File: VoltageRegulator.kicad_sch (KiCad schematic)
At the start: 16 parts, among them J1 Conn_01x02_Female, Q1 VNP10N07

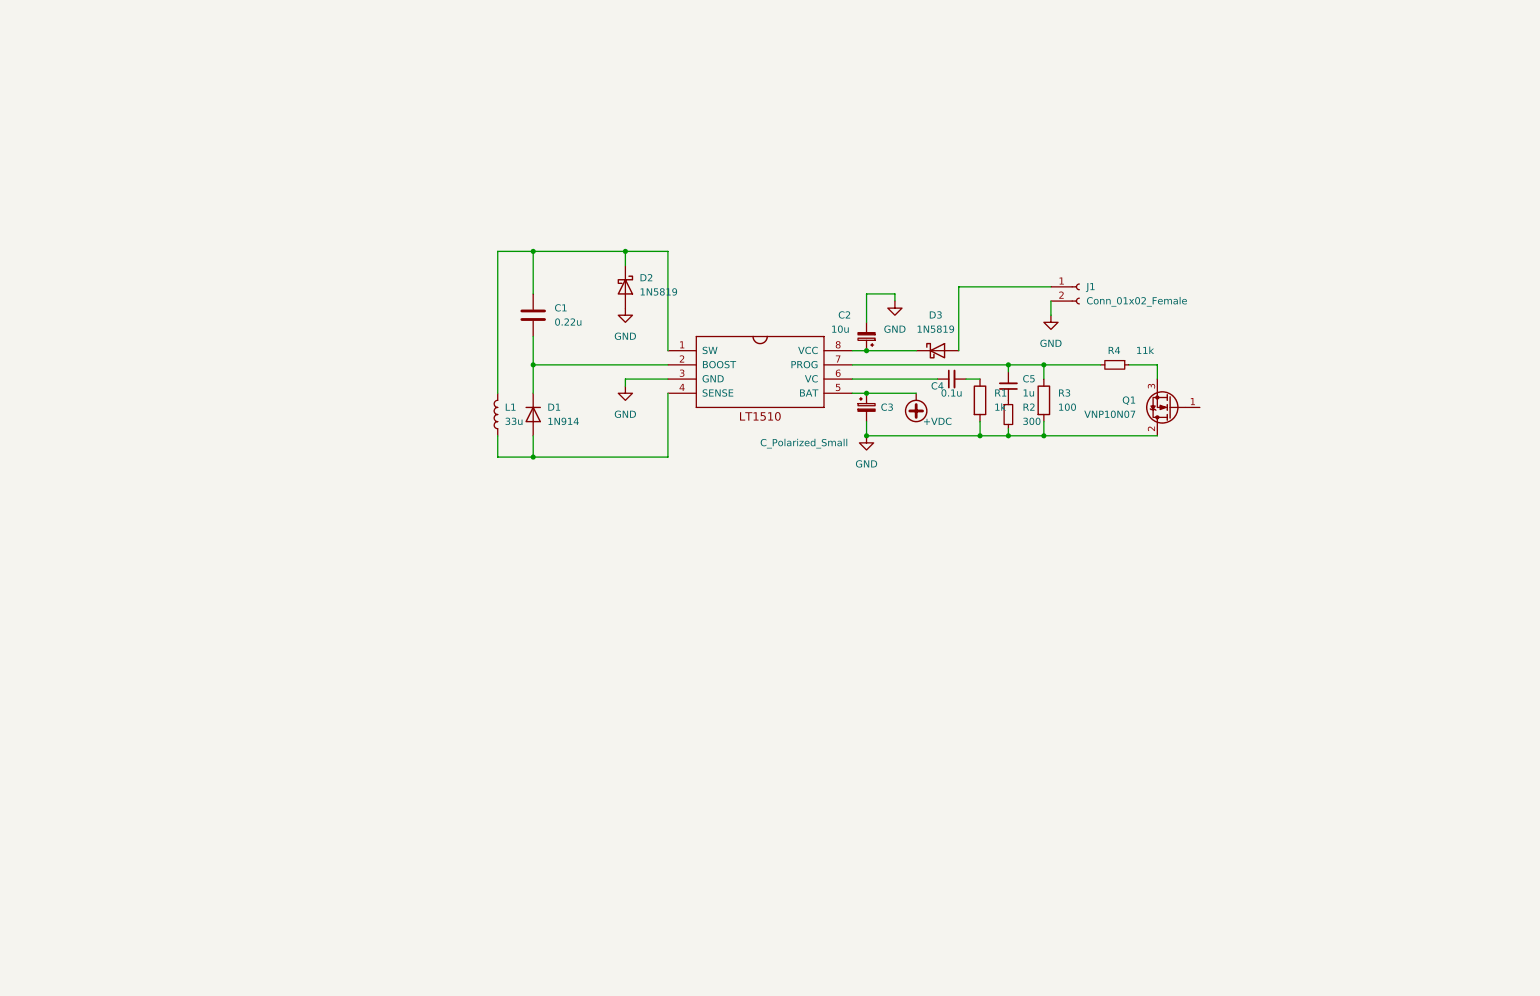
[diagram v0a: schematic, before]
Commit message: Layout almost finished
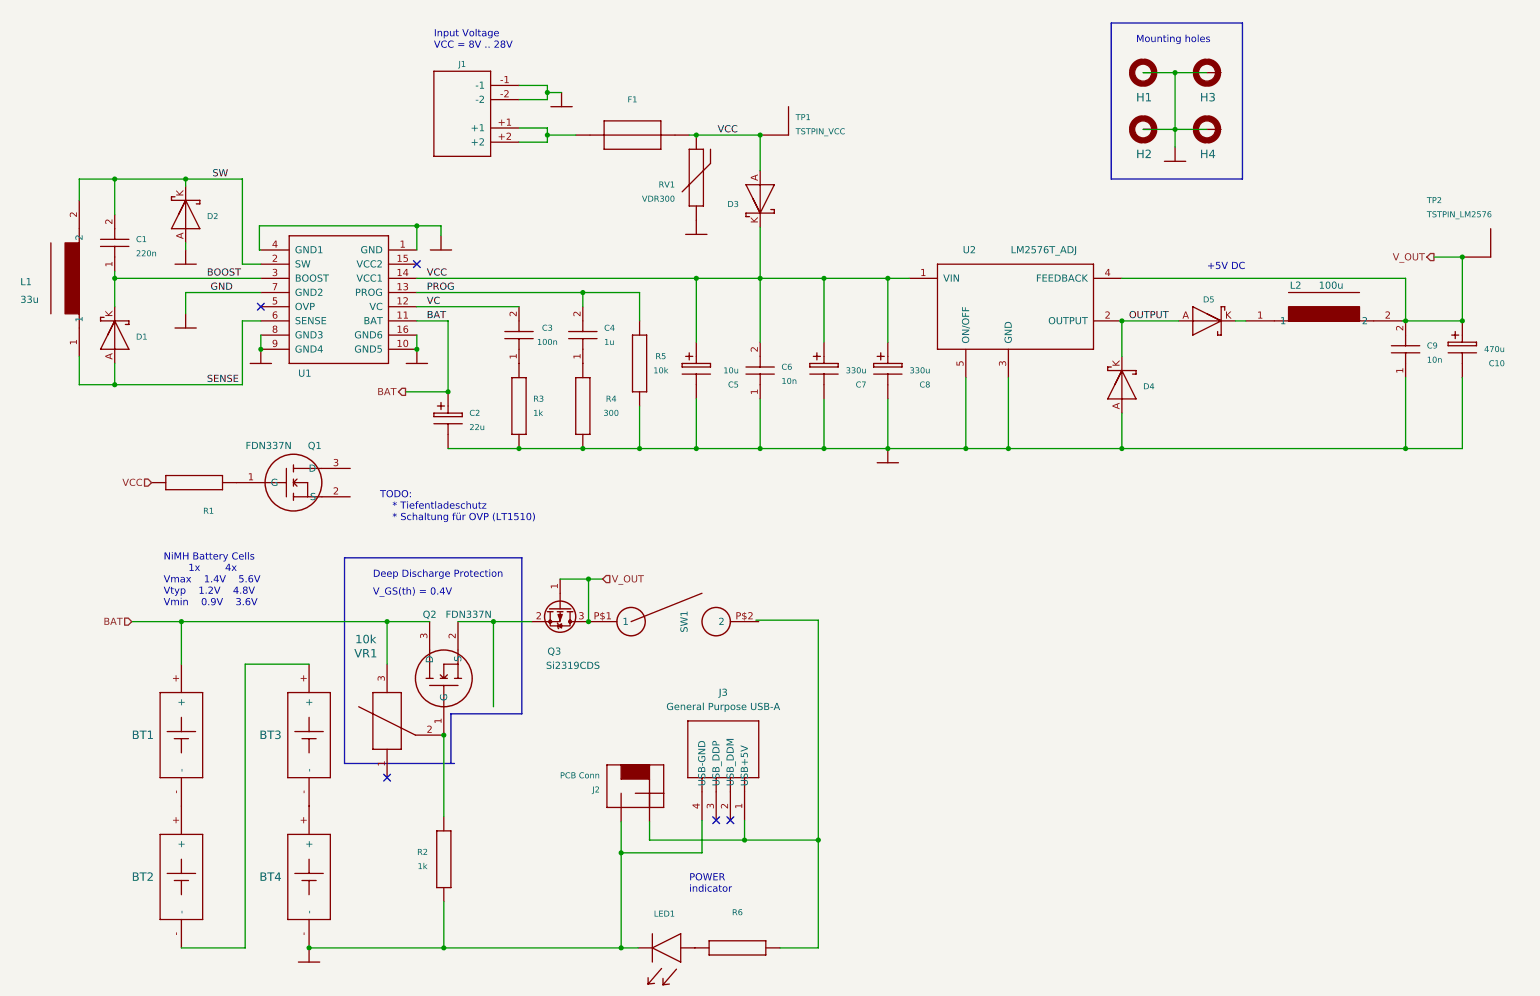
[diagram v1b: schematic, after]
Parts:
- removed 1: LT1510, symbol EmbeddedSys:LT1510
- removed C1: 0.22u, Capacitor_SMD:C_0603_1608Metric, symbol Device:C
- removed C2: 10u, Capacitor_SMD:C_0603_1608Metric, symbol Device:C_Polarized_Small
- removed C3: C_Polarized_Small, symbol Device:C_Polarized_Small
- removed C4: 0.1u, Capacitor_SMD:C_0603_1608Metric, symbol Device:C_Small
- removed C5: 1u, Capacitor_SMD:C_0603_1608Metric, symbol Device:C_Small
- removed D1: 1N914, Diode_THT:D_DO-35_SOD27_P7.62mm_Horizontal, symbol Diode:1N914
- removed D2, D3: 1N5819, Diode_THT:D_DO-41_SOD81_P10.16mm_Horizontal, symbol Diode:1N5819
- removed J1: Conn_01x02_Female, Connector_JST:JST_EH_B2B-EH-A_1x02_P2.50mm_Vertical, symbol Connector:Conn_01x02_Female
- removed L1: 33u, Capacitor_SMD:C_0603_1608Metric, symbol Device:L
- removed Q1: VNP10N07, Package_TO_SOT_THT:TO-220-3_Vertical, symbol Transistor_FET:VNP10N07
- removed R1: 1k, Resistor_SMD:R_0603_1608Metric, symbol Device:R
- removed R2: 300, Resistor_SMD:R_0603_1608Metric, symbol Device:R_Small
- removed R3: 100, Resistor_SMD:R_0603_1608Metric, symbol Device:R
- removed R4: 11k, Resistor_SMD:R_0603_1608Metric, symbol Device:R_Small
- added BT1, BT2, BT3, BT4: POWER_POWER_AKKU, LIB_Embedsys:POWER_POWER_AKKU_AA, symbol EmbeddedSys:POWER_POWER_AKKU
- added C1: 220n, LIB_Embedsys:C1206, symbol EmbeddedSys:POWER_POWER_C_SMD
- added C10: 470u, LIB_Embedsys:POWER_POWER_C-POL, symbol EmbeddedSys:POWER_POWER_C-POL{dblquote}
- added C2: 22u, LIB_Embedsys:POWER_POWER_C-POL, symbol EmbeddedSys:POWER_POWER_C-POL{dblquote}
- added C3: 100n, LIB_Embedsys:C1206, symbol EmbeddedSys:POWER_POWER_C_SMD
- added C4: 1u, LIB_Embedsys:C1206, symbol EmbeddedSys:POWER_POWER_C_SMD
- added C5: 10u, LIB_Embedsys:POWER_POWER_C-POL, symbol EmbeddedSys:POWER_POWER_C-POL{dblquote}
- added C6, C9: 10n, LIB_Embedsys:C1206, symbol EmbeddedSys:POWER_POWER_C_SMD
- added C7, C8: 330u, LIB_Embedsys:POWER_POWER_C-POL, symbol EmbeddedSys:POWER_POWER_C-POL{dblquote}
- added D1, D2, D3, D4, D5: POWER_POWER_SB560", LIB_Embedsys:POWER_POWER_DO201AD, symbol EmbeddedSys:POWER_POWER_SB560{dblquote}
- added F1: (no value), symbol EmbeddedSys:POWER_POWER_FUSE{dblquote}
- added H1, H2, H3, H4: MOUNT-PAD-3.0, LIB_Embedsys:POWER_HOLES_3,0-PAD, symbol EmbeddedSys:POWER_HOLES_MOUNT-PAD-ROUND3.0
- added J1: POWER_POWER_ROKA-PWR-IN, LIB_Embedsys:POWER_POWER_ROKA-PWR-IN, symbol EmbeddedSys:POWER_POWER_ROKA-PWR-IN
- added J2: PCB Conn, LIB_Embedsys:POWER_POWER_CON2, symbol EmbeddedSys:POWER_POWER_CON2{dblquote}
- added J3: General Purpose USB-A, LIB_Embedsys:POWER_POWER_USBA, symbol EmbeddedSys:POWER_POWER_USBA
- added L1: 33u, LIB_Embedsys:POWER_POWER_SPULE_STEHEND, symbol EmbeddedSys:POWER_POWER_SPULE_STEHEND
- added L2: 100u, LIB_Embedsys:POWER_POWER_SPULE_STEHEND, symbol EmbeddedSys:POWER_POWER_SPULE_STEHEND
- added LED1: (no value), symbol EmbeddedSys:POWER_POWER_LED-3MM
- added Q1, Q2: FDN337N, LIB_Embedsys:SOT23, symbol EmbeddedSys:FDN337N
- added Q3: Si2319CDS, Package_TO_SOT_SMD:SOT-23, symbol Transistor_FET:Si2319CDS
- added R1: (no value), LIB_Embedsys:R0805, symbol EmbeddedSys:POWER_POWER_SMD_R
- added R2, R3: 1k, LIB_Embedsys:R0805, symbol EmbeddedSys:POWER_POWER_SMD_R
- added R4: 300, LIB_Embedsys:R0805, symbol EmbeddedSys:POWER_POWER_SMD_R
- added R5: 10k, LIB_Embedsys:R0805, symbol EmbeddedSys:POWER_POWER_SMD_R
- added R6: (no value), symbol EmbeddedSys:POWER_POWER_SMD_R
- added RV1: VDR300, LIB_Embedsys:POWER_POWER_VDR, symbol EmbeddedSys:POWER_POWER_VDR300
- added SW1: POWER Switch, LIB_Embedsys:POWER_POWER_SWITCH_ON, symbol EmbeddedSys:POWER_POWER_SWITCH_ON
- added TP1: TSTPIN_VCC, LIB_Embedsys:POWER_POWER_TSTPIN, symbol EmbeddedSys:POWER_POWER_TSTPIN{dblquote}
- added TP2: TSTPIN_LM2576, LIB_Embedsys:POWER_POWER_TSTPIN, symbol EmbeddedSys:POWER_POWER_TSTPIN{dblquote}
- added U1: (no value), symbol EmbeddedSys:LT1510CN
- added U2: LM2576T_ADJ, LIB_Embedsys:POWER_POWER_5_LEAD_TO220, symbol EmbeddedSys:POWER_POWER_LM2576T_ADJ
- added VR1: 10k, LIB_Embedsys:POWER_POWER_POTI, symbol EmbeddedSys:POWER_POWER_POTI
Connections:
- net GND: now also BT4.-, C10.-, C2.-, C5.-, C6.1 (P$1), C7.-, C8.-, C9.1 (P$1), D2.A, D4.A, H1.B3,0 (MOUNT), H2.B3,0 (MOUNT), H3.B3,0 (MOUNT), H4.B3,0 (MOUNT), J1.-1, J1.-2, J2.GND, J3.4 (USB-GND), LED1.K, R2.1 (P$1), R3.1 (P$1), R4.1 (P$1), R5.1 (P$1), RV1.P$1, U1.1 (GND), U1.10 (GND5), U1.16 (GND6), U1.4 (GND1), U1.7 (GND2), U1.8 (GND3), U1.9 (GND4), U2.3 (GND), U2.5 (ON/OFF)
- new net: D5.K, L2.1
- new net: Q1.1 (G), R1.2 (P$2)
- new net: J2.+5V, J3.1 (USB+5V), R6.2 (P$2)
- new net: Q2.2 (S), Q3.2 (S)
- new net: LED1.A, R6.1 (P$1)
- new net: C4.1 (P$1), R4.2 (P$2)
- new net: BT2.-, BT3.+
- new net: BT3.-, BT4.+
- new net: F1.P$2, J1.+1, J1.+2
- new net: BT1.-, BT2.+
- new net: Q2.1 (G), R2.2 (P$2), VR1.2
- new net: C3.1 (P$1), R3.2 (P$2)
- new net BAT: BT1.+, C2.+, Q2.3 (D), U1.11 (BAT), VR1.3
- new net BOOST: C1.1 (P$1), D1.K, U1.3 (BOOST)
- new net OUTPUT: D4.K, D5.A, U2.2 (OUTPUT)
- new net PROG: C4.2 (P$2), R5.2 (P$2), U1.13 (PROG)
- new net SENSE: D1.A, L1.1, U1.6 (SENSE)
- new net SW: C1.2 (P$2), D2.K, L1.2, U1.2 (SW)
- new net VC: C3.2 (P$2), U1.12 (VC)
- new net VCC: C5.+, C6.2 (P$2), C7.+, C8.+, D3.A, D3.K, F1.P$1, R1.1 (P$1), RV1.P$2, TP1.P$1, U1.14 (VCC1), U2.1 (VIN)
- new net V_OUT: C10.+, C9.2 (P$2), L2.2, Q3.1 (G), Q3.3 (D), SW1.P$1 (1), TP2.P$1, U2.4 (FEEDBACK)
- no-connect marks 0 -> 5
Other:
- note added: "+5V DC"
- note added: "Deep Discharge Protection"
- note added: "Input Voltage VCC = 8V .. 28V"
- note added: "Mounting holes"
- note added: "NiMH Battery Cells 1x 4x Vmax 1.4V 5.6V Vtyp 1.2V 4.8V Vmin 0.9V 3.6V"
- note added: "POWER indicator"
- note added: "TODO: * Tiefentladeschutz * Schaltung für OVP (LT1510)"
- note added: "V_GS(th) = 0.4V"

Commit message: Version 1.0
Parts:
- removed BT1, BT2, BT3, BT4: POWER_POWER_AKKU, LIB_Embedsys:POWER_POWER_AKKU_AA, symbol EmbeddedSys:POWER_POWER_AKKU
- removed C1: 220n, LIB_Embedsys:C1206, symbol EmbeddedSys:POWER_POWER_C_SMD
- removed C10: 470u, LIB_Embedsys:POWER_POWER_C-POL, symbol EmbeddedSys:POWER_POWER_C-POL{dblquote}
- removed C2: 22u, LIB_Embedsys:POWER_POWER_C-POL, symbol EmbeddedSys:POWER_POWER_C-POL{dblquote}
- removed C3: 100n, LIB_Embedsys:C1206, symbol EmbeddedSys:POWER_POWER_C_SMD
- removed C4: 1u, LIB_Embedsys:C1206, symbol EmbeddedSys:POWER_POWER_C_SMD
- removed C5: 10u, LIB_Embedsys:POWER_POWER_C-POL, symbol EmbeddedSys:POWER_POWER_C-POL{dblquote}
- removed C6, C9: 10n, LIB_Embedsys:C1206, symbol EmbeddedSys:POWER_POWER_C_SMD
- removed C7, C8: 330u, LIB_Embedsys:POWER_POWER_C-POL, symbol EmbeddedSys:POWER_POWER_C-POL{dblquote}
- removed D1, D2, D3, D4, D5: POWER_POWER_SB560", LIB_Embedsys:POWER_POWER_DO201AD, symbol EmbeddedSys:POWER_POWER_SB560{dblquote}
- removed F1: (no value), symbol EmbeddedSys:POWER_POWER_FUSE{dblquote}
- removed H1, H2, H3, H4: MOUNT-PAD-3.0, LIB_Embedsys:POWER_HOLES_3,0-PAD, symbol EmbeddedSys:POWER_HOLES_MOUNT-PAD-ROUND3.0
- removed J1: POWER_POWER_ROKA-PWR-IN, LIB_Embedsys:POWER_POWER_ROKA-PWR-IN, symbol EmbeddedSys:POWER_POWER_ROKA-PWR-IN
- removed J2: PCB Conn, LIB_Embedsys:POWER_POWER_CON2, symbol EmbeddedSys:POWER_POWER_CON2{dblquote}
- removed J3: General Purpose USB-A, LIB_Embedsys:POWER_POWER_USBA, symbol EmbeddedSys:POWER_POWER_USBA
- removed L1: 33u, LIB_Embedsys:POWER_POWER_SPULE_STEHEND, symbol EmbeddedSys:POWER_POWER_SPULE_STEHEND
- removed L2: 100u, LIB_Embedsys:POWER_POWER_SPULE_STEHEND, symbol EmbeddedSys:POWER_POWER_SPULE_STEHEND
- removed LED1: (no value), symbol EmbeddedSys:POWER_POWER_LED-3MM
- removed Q1, Q2: FDN337N, LIB_Embedsys:SOT23, symbol EmbeddedSys:FDN337N
- removed Q3: Si2319CDS, Package_TO_SOT_SMD:SOT-23, symbol Transistor_FET:Si2319CDS
- removed R1: (no value), LIB_Embedsys:R0805, symbol EmbeddedSys:POWER_POWER_SMD_R
- removed R2, R3: 1k, LIB_Embedsys:R0805, symbol EmbeddedSys:POWER_POWER_SMD_R
- removed R4: 300, LIB_Embedsys:R0805, symbol EmbeddedSys:POWER_POWER_SMD_R
- removed R5: 10k, LIB_Embedsys:R0805, symbol EmbeddedSys:POWER_POWER_SMD_R
- removed R6: (no value), symbol EmbeddedSys:POWER_POWER_SMD_R
- removed RV1: VDR300, LIB_Embedsys:POWER_POWER_VDR, symbol EmbeddedSys:POWER_POWER_VDR300
- removed SW1: POWER Switch, LIB_Embedsys:POWER_POWER_SWITCH_ON, symbol EmbeddedSys:POWER_POWER_SWITCH_ON
- removed TP1: TSTPIN_VCC, LIB_Embedsys:POWER_POWER_TSTPIN, symbol EmbeddedSys:POWER_POWER_TSTPIN{dblquote}
- removed TP2: TSTPIN_LM2576, LIB_Embedsys:POWER_POWER_TSTPIN, symbol EmbeddedSys:POWER_POWER_TSTPIN{dblquote}
- removed U1: (no value), symbol EmbeddedSys:LT1510CN
- removed U2: LM2576T_ADJ, LIB_Embedsys:POWER_POWER_5_LEAD_TO220, symbol EmbeddedSys:POWER_POWER_LM2576T_ADJ
- removed VR1: 10k, LIB_Embedsys:POWER_POWER_POTI, symbol EmbeddedSys:POWER_POWER_POTI
- added AKKU1, AKKU2, AKKU3, AKKU4: 1.2V NIMH, LIB_Embedsys:POWER_POWER_AKKU_AA, symbol LIB_Embedsys:POWER_POWER_AKKU
- added C1, C2, C3, C6, C7: 100nF, LIB_Embedsys:C1206, symbol LIB_Embedsys:POWER_POWER_C_SMD
- added C4: 22uF, LIB_Embedsys:C1206, symbol LIB_Embedsys:POWER_POWER_C_SMD
- added C5: 1uF, LIB_Embedsys:C1206, symbol LIB_Embedsys:POWER_POWER_C_SMD
- added CP1, CP2, CP3: 330uF-35V, LIB_Embedsys:POWER_POWER_C-POL, symbol LIB_Embedsys:POWER_POWER_C-POL{dblquote}
- added CP4: 330uF/35V, LIB_Embedsys:POWER_POWER_C-POL, symbol LIB_Embedsys:POWER_POWER_C-POL{dblquote}
- added CP5: 10nF, LIB_Embedsys:C1206, symbol LIB_Embedsys:POWER_POWER_C_SMD
- added CP6: 470μF/25V4, LIB_Embedsys:POWER_POWER_C-POL, symbol LIB_Embedsys:POWER_POWER_C-POL{dblquote}
- added CP7, CP8, CP9: 470μF/25V, LIB_Embedsys:POWER_POWER_C-POL, symbol LIB_Embedsys:POWER_POWER_C-POL{dblquote}
- added D1, D3, D4, D6: POWER_POWER_SB560", LIB_Embedsys:POWER_POWER_DO201AD, symbol LIB_Embedsys:POWER_POWER_SB560{dblquote}
- added D2, D7, D8: 1N4148, LIB_Embedsys:C1206, symbol LIB_Embedsys:POWER_POWER_1N4148
- added D5: POWER_POWER_SB560, LIB_Embedsys:POWER_POWER_DO201AD, symbol LIB_Embedsys:POWER_POWER_SB560{dblquote}
- added D9: ZD8.2V, LIB_Embedsys:C1206, symbol LIB_Embedsys:POWER_POWER_1N4148
- added F1: POWER_POWER_FUSE", LIB_Embedsys:POWER_POWER_DIP2-300R, symbol LIB_Embedsys:POWER_POWER_FUSE{dblquote}
- added J1: POWER_POWER_ROKA-PWR-IN, LIB_Embedsys:POWER_POWER_ROKA-PWR-IN, symbol LIB_Embedsys:POWER_POWER_ROKA-PWR-IN
- added L1, L2: POWER_POWER_SPULE_STEHEND, LIB_Embedsys:POWER_POWER_SPULE_STEHEND, symbol LIB_Embedsys:POWER_POWER_SPULE_STEHEND
- added LED1: Grün-2,4V-25mA2, LIB_Embedsys:POWER_POWER_LED-3MM, symbol LIB_Embedsys:POWER_POWER_LED-3MM
- added Q1: FDN337N, LIB_Embedsys:SOT23, symbol LIB_Embedsys:FDN337N
- added Q2, Q3: BC848SMD, LIB_Embedsys:SOT23, symbol LIB_Embedsys:BC848SMD
- added Q4: SI2369, LIB_Embedsys:SOT23, symbol LIB_Embedsys:FDN337N
- added R1, R2: 100k, LIB_Embedsys:R0805, symbol LIB_Embedsys:POWER_POWER_SMD_R
- added R10, R11, R6: 10k, LIB_Embedsys:R0805, symbol LIB_Embedsys:POWER_POWER_SMD_R
- added R12, R14, R15, R7: 1M, LIB_Embedsys:R0805, symbol LIB_Embedsys:POWER_POWER_SMD_R
- added R13, R5: 1k, LIB_Embedsys:R0805, symbol LIB_Embedsys:POWER_POWER_SMD_R
- added R16, R3: 47k, LIB_Embedsys:R0805, symbol LIB_Embedsys:POWER_POWER_SMD_R
- added R4: 330, LIB_Embedsys:R0805, symbol LIB_Embedsys:POWER_POWER_SMD_R
- added R8: 0, LIB_Embedsys:R0805, symbol LIB_Embedsys:POWER_POWER_SMD_R
- added R9: 390k, LIB_Embedsys:R0805, symbol LIB_Embedsys:POWER_POWER_SMD_R
- added S1: LM2576-5T_4V-40V-max3A, LIB_Embedsys:POWER_POWER_TO-220_5_short, symbol LIB_Embedsys:POWER_POWER_LM2576-5T
- added ST1: POWER_POWER_CON2", LIB_Embedsys:POWER_POWER_CON2, symbol LIB_Embedsys:POWER_POWER_CON2{dblquote}
- added ST2: POWER_POWER_USBA, LIB_Embedsys:POWER_POWER_USBA, symbol LIB_Embedsys:POWER_POWER_USBA
- added TP1, TP10, TP11, TP2, TP3, TP4, TP5, TP6, TP7, TP8, TP9: POWER_POWER_TSTPIN", LIB_Embedsys:POWER_POWER_TSTPIN, symbol LIB_Embedsys:POWER_POWER_TSTPIN{dblquote}
- added U1: LT1510CN, LIB_Embedsys:SO16, symbol LIB_Embedsys:LT1510CN
- added U2: POWER_POWER_SWITCH_ON, LIB_Embedsys:POWER_POWER_SWITCH_ON, symbol LIB_Embedsys:POWER_POWER_SWITCH_ON
- added V1: VDR300, LIB_Embedsys:POWER_POWER_VDR, symbol LIB_Embedsys:POWER_POWER_VDR300
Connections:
- net BAT: now also C4.2 (P$2), Q1.3 (D), R8.2 (P$2), TP9.P$1, U1.11 (BAT), U2.P$1 (1)
- net BOOST: now also C1.1 (P$1), C2.1 (P$1), D2.2 (K), TP3.P$1, U1.3 (BOOST)
- net GND: now also AKKU1.-, C3.1 (P$1), C4.1 (P$1), C6.2 (P$2), C7.1 (P$1), CP1.-, CP2.-, CP3.-, CP4.-, CP5.2 (P$2), CP6.-, CP7.-, CP8.-, CP9.-, D1.A, D6.A, J1.-1, J1.-2, LED1.K, Q2.2 (E), Q3.2 (E), R1.1 (P$1), R11.1 (P$1), R16.1 (P$1), R4.2 (P$2), R6.2 (P$2), S1.3 (GND), S1.5 (\~{ON/OFF}), ST1.GND, ST2.4 (USB-GND), TP11.P$1, U1.1 (GND), U1.10 (GND5), U1.16 (GND6), U1.4 (GND1), U1.7 (GND2), U1.8 (GND3), U1.9 (GND4), V1.P$1
- net PROG: now also C5.1 (P$1), R6.1 (P$1), TP6.P$1, U1.13 (PROG)
- net SENSE: now also D2.1 (A), L1.1, TP5.P$1, U1.6 (SENSE)
- net VC: now also R5.2 (P$2), TP7.P$1, U1.12 (VC)
- net VCC: now also C3.2 (P$2), CP4.+, D4.K, R7.2 (P$2), TP4.P$1, U1.14 (VCC1), U1.15 (VCC2)
- new net: Q2.3 (C), Q3.1 (B), R9.2 (P$2)
- new net: Q3.3 (C), Q4.1 (G), R12.1 (P$1)
- new net: C1.2 (P$2), C2.2 (P$2), D1.K, L1.2, TP1.P$1, U1.2 (SW)
- new net: D7.2 (K), D8.1 (A)
- new net: D8.2 (K), R9.1 (P$1)
- new net: AKKU2.+, AKKU3.-
- new net: AKKU1.+, AKKU2.-
- new net: AKKU4.+, R8.1 (P$1)
- new net: AKKU3.+, AKKU4.-
- new net: C6.1 (P$1), R5.1 (P$1)
- new net: C7.2 (P$2), CP6.+, CP7.+, CP8.+, CP9.+, L2.2, Q4.3 (D), R13.2 (P$2), R14.2 (P$2), S1.4 (FEEDBACK), ST1.+5V, ST2.1 (USB+5V), TP10.P$1
- new net: Q2.1 (B), R10.1 (P$1), R11.2 (P$2)
- new net: D9.1 (A), R10.2 (P$2)
- new net: D5.A, S1.2 (OUT), TP8.P$1
- new net: D7.1 (A), Q4.2 (S), R12.2 (P$2), U2.P$2 (2)
- new net: F1.P$1, J1.+1, J1.+2, TP2.P$1
- new net: D3.A, D4.A, F1.P$2, V1.P$2
- new net: LED1.A, R13.1 (P$1)
- new net: R15.1 (P$1), R16.2 (P$2)
- new net: D5.K, D6.K, L2.1
- new net: R1.2 (P$2), R2.1 (P$1), U1.5 (OVP)
- new net: R2.2 (P$2), R3.1 (P$1)
- new net: Q1.2 (S), R3.2 (P$2)
- new net: Q1.1 (G), R7.1 (P$1)
- new net: R14.1 (P$1), R15.2 (P$2)
- new net: C5.2 (P$2), R4.1 (P$1)
- new net +VIN: CP1.+, CP2.+, CP3.+, CP5.1 (P$1), D3.K, D9.2 (K), S1.1 (+VIN)
- no-connect marks 5 -> 2
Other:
- note added: "2.465V"
- note removed: "+5V DC"
- note removed: "Deep Discharge Protection"
- note removed: "Mounting holes"
- note removed: "NiMH Battery Cells 1x 4x Vmax 1.4V 5.6V Vtyp 1.2V 4.8V Vmin 0.9V 3.6V"
- note removed: "POWER indicator"
- note removed: "TODO: * Tiefentladeschutz * Schaltung für OVP (LT1510)"
- note removed: "V_GS(th) = 0.4V"
- company: (none) -> Marco Dittmann
- title: DC-Voltage-Regulator -> DC-Voltage Regulator
